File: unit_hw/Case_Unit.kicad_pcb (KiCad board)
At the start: 2 copper layers, 16.1 x 33.6 mm, 17 parts, among them J1 Conn_01x02, J2 Conn_01x04, J3 RJ45, J4 Conn_01x03, Q1 2N7002, U1 SPX3819M5-L-3-3, U2 STM32G030F6Px, U3 MAX487E

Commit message: Revise unit schematic
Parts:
- removed the J1 at (66.7, 46.0)
- removed Q1: 2N7002, Package_TO_SOT_SMD:SOT-23
- moved C4 5.72 mm to (78.5, 43.5), turned to 0 degrees
- moved R2 5.22 mm to (80.5, 46.9), turned to -90 degrees
- moved C1 2.50 mm to (70.7, 45.8)
- moved C2 2.50 mm to (70.7, 47.6)
- moved U1 2.50 mm to (68.2, 46.7)
- moved R1 1.56 mm to (77.3, 37.8), turned to 90 degrees
- moved J3 1.50 mm to (68.8, 53.7)
- moved U3 1.01 mm to (76.4, 46.7), turned to 0 degrees
- renumbered J2 to J1
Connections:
- J3 pad 1: unconnected-(J3-Pad1) -> +5V
- J3 pad 2: unconnected-(J3-Pad2) -> GND
- U2 pad 12: /MAX487_RE -> unconnected-(U2-PA5-Pad12)
- U2 pad 14: /SERVO_OUT_MCU -> /SERVO_OUT
- U3 pad 2: /MAX487_RE -> /MAX487_DE
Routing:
- net +5V: track 41.9 -> 6.01 mm
- net /MAX487_DE: track 4.78 -> 14.9 mm
- net /UART_RX: track 13.2 -> 6.63 mm
- net /MAX487_RE: track 6.47 -> 0.00 mm
- net /RS422+: track 6.16 -> 0.00 mm
- net /SERVO_OUT: track 5.28 -> 0.00 mm
- net GND: track 11.6 -> 6.40 mm, vias 8 -> 5
- net /UART_TX: track 8.40 -> 13.0 mm
- net /RS422-: track 3.62 -> 0.00 mm
- net +3V3: track 20.7 -> 17.9 mm
- net /SERVO_OUT_MCU: track 2.36 -> 0.00 mm

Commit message: Submit for fab (Rev. 2 unit)
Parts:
- added C3: 22u, Capacitor_SMD:C_0603_1608Metric, F.Cu at (69.5, 40.0)
- added C4: 22u, Capacitor_SMD:C_0603_1608Metric, F.Cu at (69.5, 38.5)
- added C5: 100n, Capacitor_SMD:C_0402_1005Metric, F.Cu at (68.9, 41.3)
- added L1: 10u, Inductor_SMD:L_Changjiang_FNR5030S, F.Cu at (72.6, 43.6)
- added R2: 100k, Resistor_SMD:R_0402_1005Metric, F.Cu at (66.1, 41.2)
- added R3: 13k, Resistor_SMD:R_0402_1005Metric, F.Cu at (66.6, 39.8)
- C1: value 4.7u -> 100n
- C2: value 10n -> 22u; footprint Capacitor_SMD:C_0402_1005Metric -> Capacitor_SMD:C_0603_1608Metric
- R1: value 4.7k -> 1
- U1: value SPX3819M5-L-3-3 -> MT2492; footprint Package_TO_SOT_SMD:SOT-23-5 -> Package_TO_SOT_SMD:SOT-23-6
- U2: value STM32G030F6Px -> PY32F003F18U6; footprint Package_SO:TSSOP-20_4.4x6.5mm_P0.65mm -> Package_DFN_QFN:QFN-20-1EP_3x3mm_P0.4mm_EP1.65x1.65mm
- moved R1 13.8 mm to (67.8, 47.8), turned to 0 degrees
- moved C6 8.42 mm to (73.6, 36.0), turned to 90 degrees
- moved U2 6.38 mm to (76.3, 37.4), turned to -90 degrees
- moved J3 5.15 mm to (75.6, 33.3), turned to -90 degrees
- moved C1 5.10 mm to (66.0, 47.8), turned to 180 degrees
- moved C7 4.88 mm to (80.0, 48.2), turned to 180 degrees
- moved R4 4.87 mm to (78.9, 38.9), turned to -90 degrees
- moved C2 3.79 mm to (67.0, 46.6), turned to 180 degrees
- moved U3 3.29 mm to (78.2, 44.0), turned to -90 degrees
- moved U1 2.94 mm to (67.5, 43.8), turned to -90 degrees
- moved R5 2.83 mm to (78.0, 48.2), turned to 180 degrees
- moved J1 1.55 mm to (69.0, 36.1)
- moved J2 0.82 mm to (68.6, 52.9)
- moved G*** 0.53 mm to (70.8, 41.6)
- moved G*** 0.53 mm to (70.6, 36.6)
- renumbered C3 to C6, C4 to C7, J3 to J2, J4 to J3, R3 to R4, R2 to R5
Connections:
- C1 pad 1: +3V3 -> VIN
- C2 pad 1: Net-(U1-BP) -> Net-(U1-EN)
- C6 pad 1: +3V3 -> +5V
- J1 pad 1: +3V3 -> +5V
- J2 pad 1: +5V -> VIN
- J2 pad 3: unconnected-(J3-Pad3) -> GND
- J2 pad 4: unconnected-(J3-Pad4) -> GND
- J2 pad 5: unconnected-(J3-Pad5) -> GND
- J2 pad 6: unconnected-(J3-Pad6) -> GND
- R1 pad 1: +5V -> VIN
- R1 pad 2: /SERVO_OUT -> Net-(U1-EN)
- U1 pad 1: +5V -> Net-(U1-BS)
- U1 pad 3: +5V -> Net-(U1-FB)
- U1 pad 4: Net-(U1-BP) -> Net-(U1-EN)
- U1 pad 5: +3V3 -> Net-(U1-EN)
- U2 pad 10: /UART_RX -> unconnected-(U2-PB6-Pad10)
- U2 pad 11: /MAX487_DE -> unconnected-(U2-PB7-Pad11)
- U2 pad 14: /SERVO_OUT -> unconnected-(U2-PF1-Pad14)
- U2 pad 17: unconnected-(U2-PA12/PA10-Pad17) -> /MAX487_DE
- U2 pad 18: /SWDIO -> /UART_TX
- U2 pad 19: /SWCLK -> /UART_RX
- U2 pad 3: unconnected-(U2-PC15-Pad3) -> /SERVO_OUT
- U2 pad 4: +3V3 -> GND
- U2 pad 5: GND -> unconnected-(U2-PA12-Pad5)
- U2 pad 6: unconnected-(U2-NRST-Pad6) -> +5V
- U2 pad 7: unconnected-(U2-PA0-Pad7) -> /SWDIO
- U2 pad 8: unconnected-(U2-PA1-Pad8) -> /SWCLK
- U2 pad 9: /UART_TX -> unconnected-(U2-PB5-Pad9)
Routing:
- net +5V: track 6.01 -> 45.8 mm
- net +3V3: track 17.9 -> 0.00 mm
- net /MAX487_DE: track 14.9 -> 6.28 mm
- net /RS422+: track 0.00 -> 7.00 mm
- net VIN: track 0.00 -> 6.48 mm
- net GND: track 6.40 -> 11.7 mm, vias 5 -> 34
- net /RS422-: track 0.00 -> 4.46 mm
- net Net-(U1-SW): track 0.00 -> 4.08 mm
- net /SERVO_OUT: track 0.00 -> 2.79 mm
- net Net-(U1-FB): track 0.00 -> 2.35 mm
- net /UART_TX: track 13.0 -> 10.8 mm
- net Net-(U1-BP): track 1.58 -> 0.00 mm
- net /SWCLK: track 3.60 -> 5.14 mm
- net Net-(U1-BS): track 0.00 -> 1.38 mm
- net /SWDIO: track 4.21 -> 2.97 mm
- added copper zone on F.Cu, net +5V
- added copper zone on F.Cu, net Net-(U1-EN)
- added copper zone on F.Cu, net Net-(U1-SW)
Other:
- board size 16.1 x 33.6 mm -> 16 x 34 mm
- board text added: "Rev. 2"
- board text removed: "JLCJLCJLCJLC"
- board text removed: "Rev. 1"

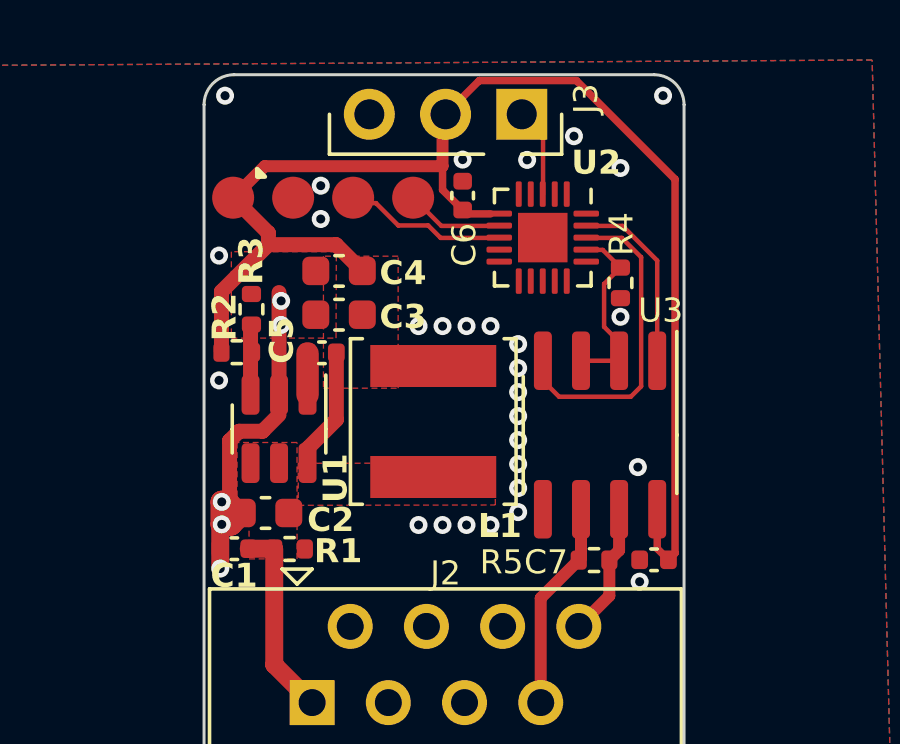
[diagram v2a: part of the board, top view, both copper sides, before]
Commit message: Revise unit board (change PY32 model to 002B; add crystal)
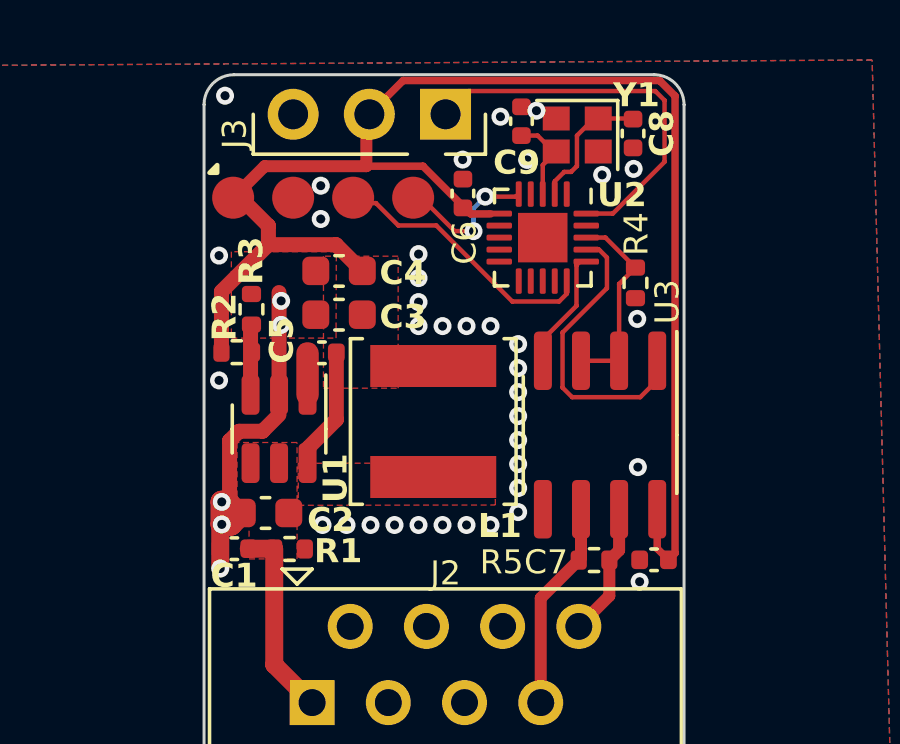
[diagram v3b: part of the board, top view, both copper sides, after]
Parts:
- added C8: 10p, Capacitor_SMD:C_0402_1005Metric, F.Cu at (79.3, 34.0)
- added C9: 10p, Capacitor_SMD:C_0402_1005Metric, F.Cu at (75.6, 33.5)
- added Y1: 24MHz 8pF, Crystal:Crystal_SMD_2016-4Pin_2.0x1.6mm, F.Cu at (77.4, 34.0)
- U2: value PY32F003F18U6 -> PY32F002BF15U6
- moved J3 2.54 mm to (73.0, 33.3)
- moved R4 0.50 mm to (79.4, 38.9)
- moved C6 0.07 mm to (73.6, 36.0)
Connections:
- U2 pad 15: unconnected-(U2-PF2-Pad15) -> /SWCLK
- U2 pad 16: unconnected-(U2-PA0-Pad16) -> /UART_TX
- U2 pad 17: /MAX487_DE -> /UART_RX
- U2 pad 18: /UART_TX -> /MAX487_DE
- U2 pad 19: /UART_RX -> unconnected-(U2-PA6-Pad19)
- U2 pad 2: unconnected-(U2-PA6-Pad2) -> Net-(U2-PC1)
- U2 pad 20: unconnected-(U2-PA4-Pad20) -> /SERVO_OUT
- U2 pad 3: /SERVO_OUT -> Net-(U2-PB7)
- U2 pad 5: unconnected-(U2-PA12-Pad5) -> /SWDIO
- U2 pad 7: /SWDIO -> unconnected-(U2-PB5-Pad7)
- U2 pad 8: /SWCLK -> unconnected-(U2-PB4-Pad8)
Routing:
- net /SERVO_OUT: track 2.79 -> 13.3 mm
- net /UART_TX: track 10.8 -> 4.03 mm
- net Net-(U2-PC1): track 0.00 -> 4.51 mm
- net /SWCLK: track 5.14 -> 9.08 mm
- net +5V: track 45.8 -> 49.4 mm
- net /UART_RX: track 6.47 -> 9.92 mm
- net Net-(U2-PB7): track 0.00 -> 2.99 mm
- net /SWDIO: track 2.97 -> 4.94 mm, vias 0 -> 2
- net GND: vias 34 -> 42
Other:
- board text added: "To build final board: - Round tracks - Fix junction at (70.41, 35.05) - one track's width 0.25 -> 0.4 - Add teardrops - Refill - DRC"

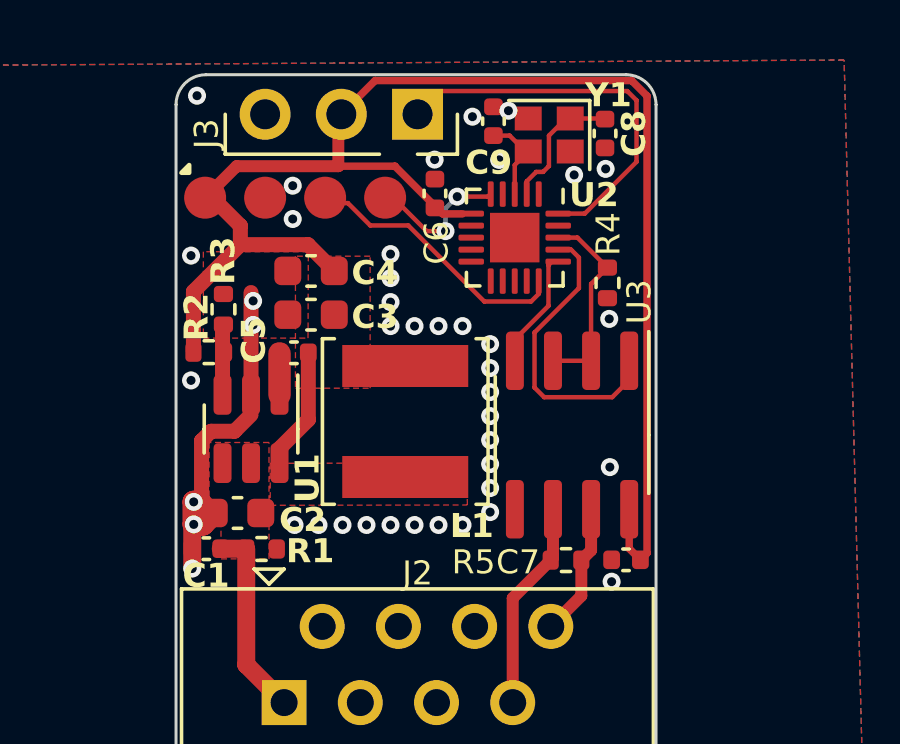
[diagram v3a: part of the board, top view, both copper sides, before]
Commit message: Finish unit redesign; submit for fab (Rev. 2 unit)
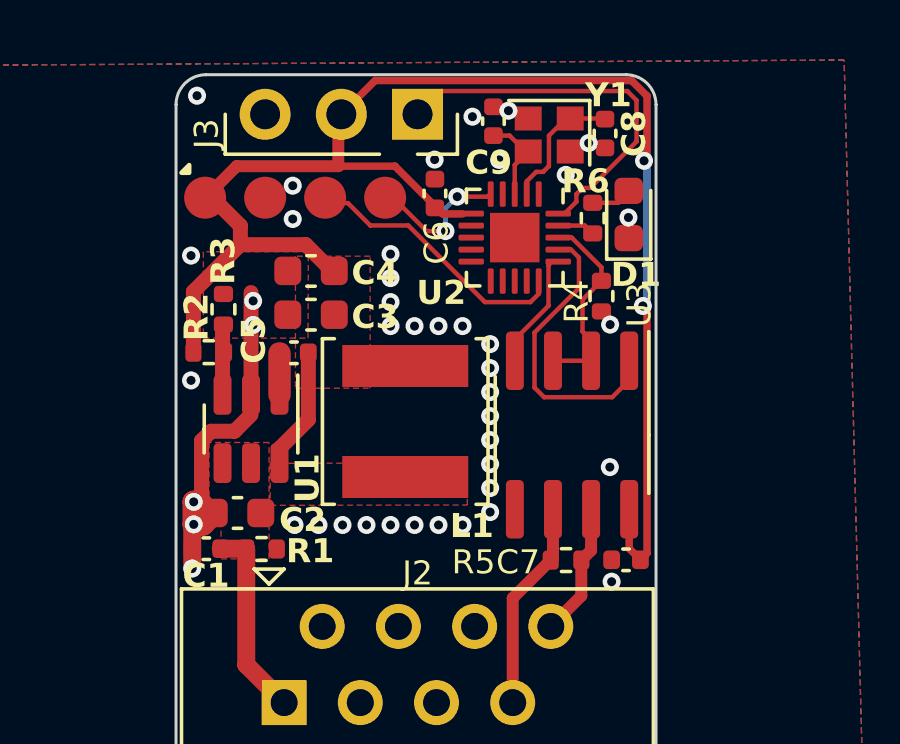
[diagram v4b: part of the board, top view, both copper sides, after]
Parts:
- added D1: White, LED_SMD:LED_0603_1608Metric, F.Cu at (80.1, 36.7)
- added R6: 7.5k, Resistor_SMD:R_0402_1005Metric, F.Cu at (78.9, 36.8)
- moved R4 0.48 mm to (79.2, 39.4)
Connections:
- U2 pad 19: unconnected-(U2-PA6-Pad19) -> /ACT_LED
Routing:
- net Net-(D1-A): track 0.00 -> 1.26 mm
- net /ACT_LED: track 0.00 -> 1.26 mm
- net +5V: track 49.4 -> 49.6 mm, vias 0 -> 2
- net GND: vias 42 -> 43
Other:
- board text added: "To build final board: - Round tracks - Fix junction at (70.41, 35.05) - one horizontal track's width 0.25 -> 0.4 - Add teardrops - Refill - DRC"
- board text removed: "To build final board: - Round tracks - Fix junction at (70.41, 35.05) - one track's width 0.25 -> 0.4 - Add teardrops - Refill - DRC"
